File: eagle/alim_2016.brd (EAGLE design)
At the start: 77 x 50 mm, 71 parts, among them J1 AVR_SPI_PRG_6PTH, U1 3.3V, U4 LM2596S-ADJ, U6 ATMEGA328P_TQFP

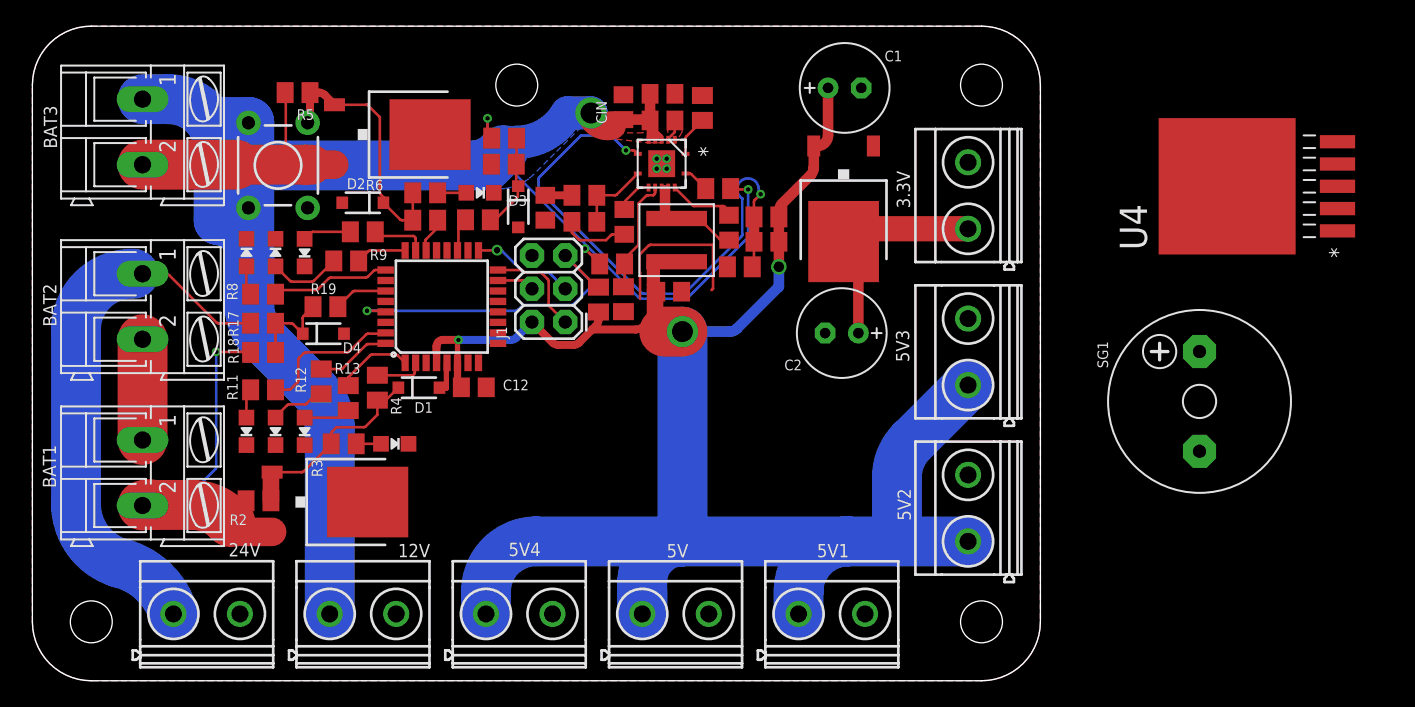
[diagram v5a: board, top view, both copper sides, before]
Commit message: changed connectors
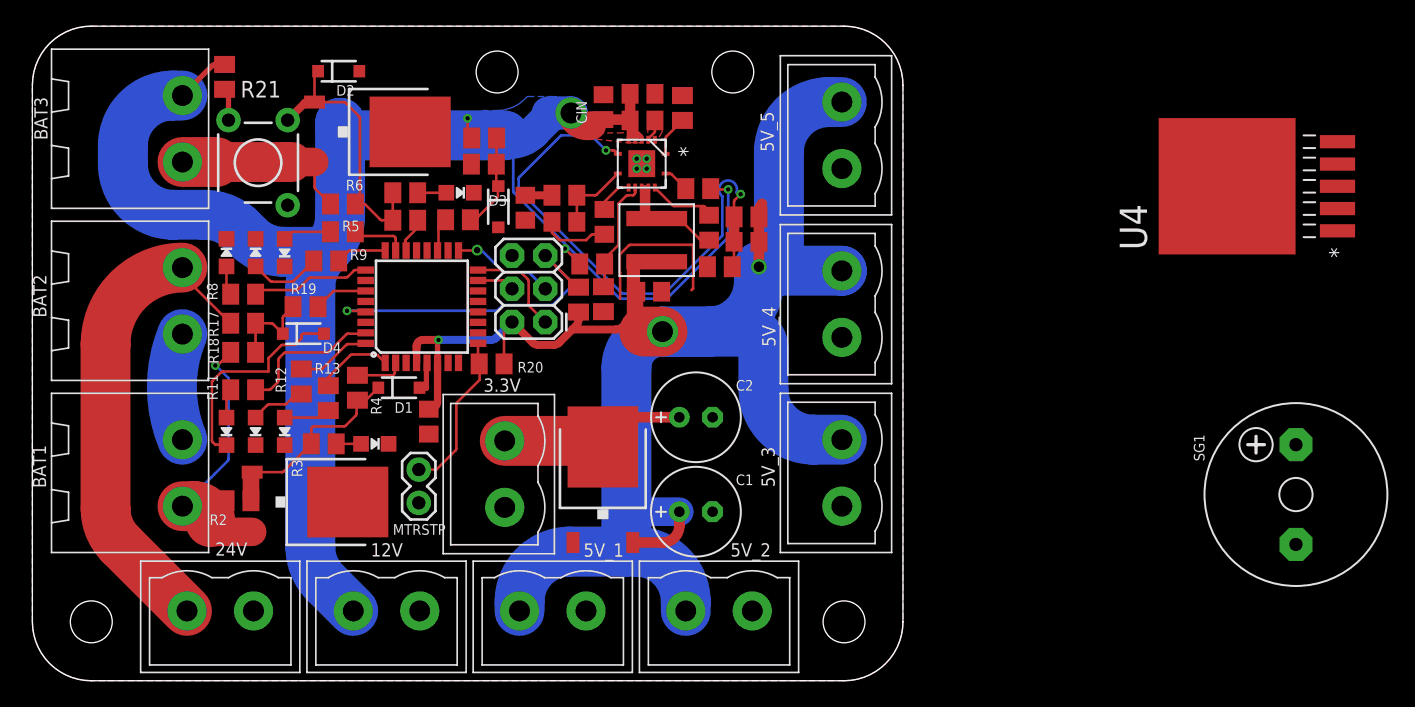
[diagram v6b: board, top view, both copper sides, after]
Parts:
- removed 5V, 5V1, 5V2, 5V3, 5V4: MKDSN1,5/2-5,08, con-phoenix-508:MKDSN1,5/2-5,08
- added 5V_1, 5V_2, 5V_3, 5V_4, 5V_5: WURTH_2PIN311, alim:WURTH311
- added MTRSTP: M02PTH, SparkFun-Connectors:1X02
- added R20, R21: 10K, resistor:M0805
- 12V, 24V, 3.3V: value MKDSN1,5/2-5,08 -> WURTH_2PIN311; device con-phoenix-508:MKDSN1,5/2-5,08 -> alim:WURTH311
- BAT1, BAT2, BAT3: value (none) -> WURTH_2PIN313; device con-ptr500:AK300/2 -> alim:WURTH313_2
- S1: value SWITCH-MOMENTARY-2PTH -> MOMENTARY-SWITCH3LEG; device SparkFun-Electromechanical:TACTILE-PTH -> alim:3LEGGED-TACT
- moved 3.3V 41.3 mm to (36.1, 15.8), turned to 270 degrees
- moved C1 34.3 mm to (50.7, 12.9)
- moved U1 27.7 mm to (43.6, 15.4), turned to 0 degrees
- moved C2 12.9 mm to (50.7, 20.1), turned to 0 degrees
- moved SG1 10.2 mm to (96.5, 14.2)
- moved D2 10.2 mm to (23.4, 46.6), turned to 0 degrees
- moved R5 9.19 mm to (23.7, 36.4)
- moved C12 4.32 mm to (30.3, 19.8), turned to 270 degrees
- moved BAT2 3.08 mm to (11.5, 29.0)
- moved BAT3 3.06 mm to (11.5, 42.2)
- moved BAT1 3.05 mm to (11.5, 15.9)
- moved 12V 1.80 mm to (27.1, 5.33)
- moved S1 1.54 mm to (17.2, 39.6)
- moved U$38 1.54 mm to (26.4, 41.9)
- moved C8 1.52 mm to (43.7, 35.1)
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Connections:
- new net N$6: MTRSTP.1, R20.2, U6.9
- new net N$7: R21.2, S1.3
- net 12V: now also 12V.P$1, BAT3.P$1, R21.1; no longer 12V.1, BAT3.1, S1.3
- net 24V: now also 24V.P$1, BAT2.P$1; no longer 24V.1, BAT2.1
- net 5.0V: now also 5V_1.P$1, 5V_2.P$1, 5V_3.P$1, 5V_4.P$1, 5V_5.P$1, R20.1; no longer 5V.1, 5V1.1, 5V2.1, 5V3.1, 5V4.1
- net GND: now also 12V.P$2, 24V.P$2, 3.3V.P$2, 5V_1.P$2, 5V_2.P$2, 5V_3.P$2, 5V_4.P$2, 5V_5.P$2, MTRSTP.2; no longer 12V.2, 24V.2, 3.3V.2, 5V.2, 5V1.2, 5V2.2, 5V3.2, 5V4.2
- net N$1: now also 3.3V.P$1; no longer 3.3V.1
- net N$13: now also BAT3.P$2; no longer BAT3.2
- net N$5: now also BAT1.P$1, BAT2.P$2; no longer BAT1.1, BAT2.2
- net N$8: now also BAT1.P$2; no longer BAT1.2
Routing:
- net GND: track 22.8 -> 39.4 mm
- net N$6: track 0.00 -> 13.1 mm
- net N$8: track 31.3 -> 23.7 mm
- net N$13: track 22.7 -> 16.4 mm
- net 24V: track 41.3 -> 36.8 mm
- net 5.0V: track 147.1 -> 143.1 mm
- net N$1: track 18.4 -> 15.0 mm
- net N$7: track 0.00 -> 2.48 mm
- net BAT12_CUT: track 20.1 -> 21.5 mm
- net BAT24_CUT: track 15.4 -> 15.9 mm
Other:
- board size 77 x 50 mm -> 66.5 x 50 mm

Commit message: shuffle things around
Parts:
- moved R21 18.3 mm to (32.3, 41.2), turned to 180 degrees
- moved S1 16.1 mm to (32.2, 45.6), turned to 0 degrees
- moved LED7 14.0 mm to (21.6, 45.8), turned to 180 degrees
- moved R6 9.89 mm to (23.7, 45.9), turned to 270 degrees
- moved R5 8.44 mm to (15.7, 39.0)
- moved U$38 5.69 mm to (21.5, 39.0)
- moved R14 4.53 mm to (31.5, 38.1), turned to 90 degrees
- moved R7 3.07 mm to (29.4, 38.1), turned to 270 degrees
- moved D2 2.44 mm to (25.8, 45.9), turned to 90 degrees
- moved R15 1.64 mm to (33.6, 38.1), turned to 270 degrees
- moved R10 1.31 mm to (22.4, 34.1)
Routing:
- net 12V: track 142.4 -> 123.4 mm
- net N$13: track 16.4 -> 10.1 mm
- net BAT12_CUT: track 21.5 -> 25.3 mm
- net N$10: track 2.19 -> 0.00 mm
- net N$23: track 2.71 -> 4.63 mm
- net N$17: track 3.70 -> 2.41 mm
- net N$22: track 4.20 -> 5.39 mm
- net N$7: track 2.48 -> 3.25 mm
- net BAT12_SENSE: track 7.57 -> 8.10 mm
- removed copper zone on layer 16, net 12V

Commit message: final version
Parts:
- removed SG1: F/CM12P, buzzer:F/CM12P
- removed U$38: IRFR8314TRPBF, alim:DPACK_1
- removed U6: ATMEGA328P_TQFP, SparkFun-DigitalIC:TQFP32-08
- added U5: 3.3V, microbuilder:TO252
- C1: device rcl:E2,5-7 -> rcl:C0805
- D1, D2, D3, D4: value (none) -> 5V
- R10, R13: value 1K -> 160
- R11, R3, R6, R8: value 1K -> 200
- R12, R9: value 1K -> 180
- R14: value 1K -> 21K
- R15: value 1K -> 13.7K
- R17: value 1K -> 51.1K
- R18: value 1K -> 10.2K
- R21: value 10K -> 21K
- R5: value 10K -> 13.7K
- U1: value 3.3V -> ATMEGA328P_TQFP; device microbuilder:TO252 -> SparkFun-DigitalIC:TQFP32-08
- U4: value LM2596S-ADJ -> IRFR8314TRPBF; device alim:TO170P1435X457-6N -> alim:DPACK_1
- moved U4 70.0 mm to (21.5, 39.0), turned to 270 degrees
- moved U1 19.1 mm to (29.7, 28.6), turned to 90 degrees
- moved C1 11.2 mm to (43.9, 21.7), turned to 90 degrees
- moved C2 7.00 mm to (51.1, 13.1)
- moved 5V_3 0.89 mm to (60.9, 15.9), turned to 90 degrees
- moved 5V_4 0.89 mm to (60.9, 28.8), turned to 90 degrees
- moved 5V_5 0.89 mm to (60.9, 41.7), turned to 90 degrees
- moved LED7 0.80 mm to (22.4, 45.8)
- moved D2 0.80 mm to (26.6, 45.9)
- moved R6 0.80 mm to (24.5, 45.9)
- moved 3.3V 0.76 mm to (35.3, 15.8), turned to 90 degrees
- moved RENT 0.25 mm to (42.8, 32.1)
- moved R16 0.23 mm to (32.5, 35.0)
- moved CCOMP3 0.20 mm to (54.7, 33.5)
- moved RFBT 0.20 mm to (54.7, 35.4)
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- renumbered C12 to C3, C8 to C4, S1 to BOOT, U$35 to L1, U$39 to U3, U$6 to U2
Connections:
- removed net VIN: U4.1
- net 5.0V: now also C1.1, U1.4, U1.6, U5.2; no longer C1.+, U1.2, U6.4, U6.6
- net BAT12_CUT: now also U4.1; no longer U$38.1
- net GND: now also C1.2, U1.3, U1.5, U4.PAD, U5.1; no longer C1.-, U$38.PAD, U1.1, U4.3, U4.6, U6.3, U6.5
- net N$1: now also U5.3; no longer U1.3
- net N$11: now also U1.2; no longer U6.2
- net N$13: now also U4.3; no longer U$38.3
- net N$14: now also U1.24; no longer U6.24
- net N$2: now also U1.17; no longer U6.17
- net N$21: now also U1.25; no longer U6.25
- net N$22: now also U1.23; no longer U6.23
- net N$23: now also U1.22; no longer U6.22
- net N$24: now also U1.1; no longer U6.1
- net N$25: now also U1.32; no longer U6.32
- net N$26: now also U1.31; no longer U6.31
- net N$27: now also U1.19; no longer U6.19
- net N$28: now also U1.27; no longer U6.27
- net N$3: now also U1.16; no longer U6.16
- net N$4: now also U1.15; no longer U6.15
- net N$6: now also U1.9; no longer U6.9
- net RESET: now also U1.29; no longer U6.29
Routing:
- net VSENSE: track 41.3 -> 48.5 mm
- net 12V: track 123.4 -> 128.0 mm
- net 5.0V: track 143.1 -> 146.0 mm
- net N$10: track 0.00 -> 2.06 mm
- net N$17: track 2.41 -> 3.75 mm
- net N$13: track 10.1 -> 10.7 mm
- net GND: vias 4 -> 13
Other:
- board text added: "+"
- board text added: "-"
- board text added: "12V unreg."
- board text added: "2015-2016"
- board text added: "24V unreg."
- board text added: "3.3V reg <.8A"
- board text added: "5V regulated <8A"
- board text added: "Carte alim"
- board text added: "LiPo 11.1-12.6V"
- board text added: "NantRobot"
- board text added: "NiMH 9-15V"
- board text removed: "Alimentation"
- board text removed: "NantRobot 2016"
